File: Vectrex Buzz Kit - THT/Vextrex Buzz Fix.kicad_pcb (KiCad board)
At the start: 2 copper layers, 22.9 x 41.7 mm, 11 parts

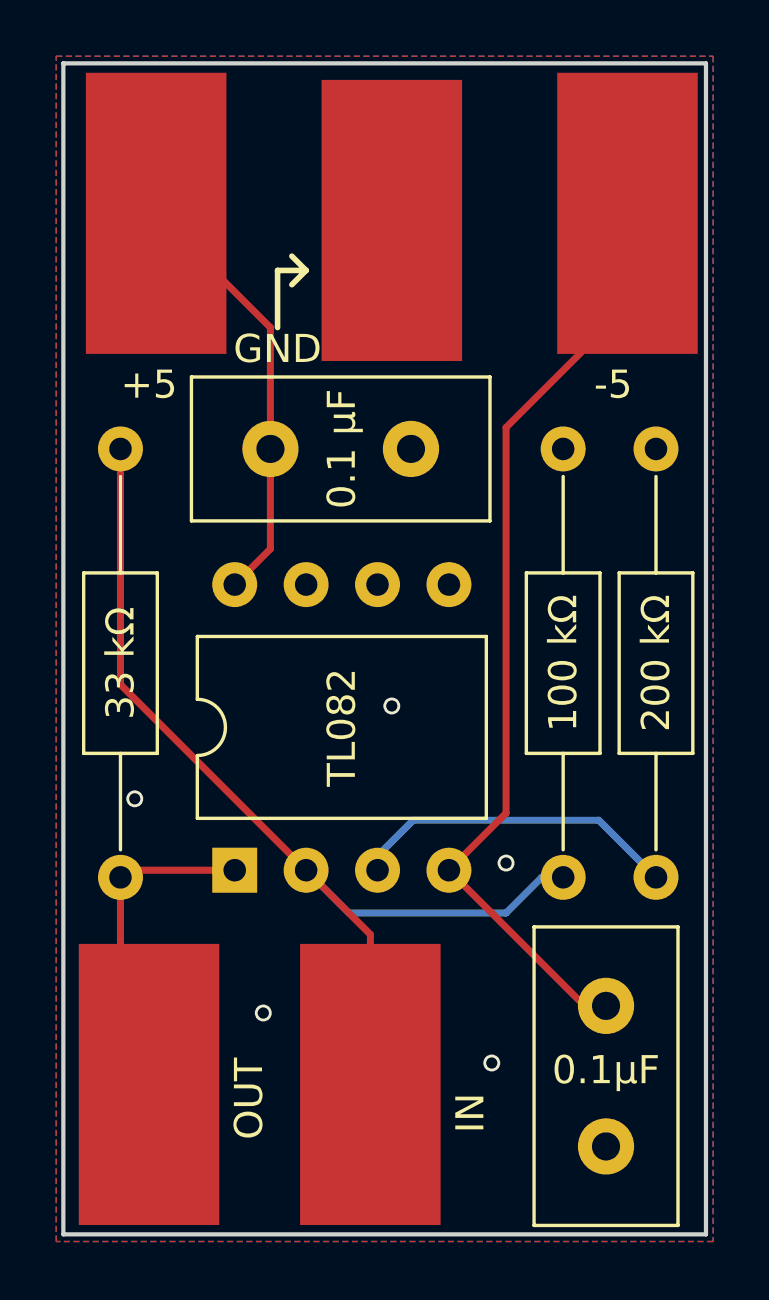
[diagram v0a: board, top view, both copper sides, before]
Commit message: Fixed Unintentional Antenna
Thanks to mobiusstriptech for the fix, applied to both SMD and THT versions.
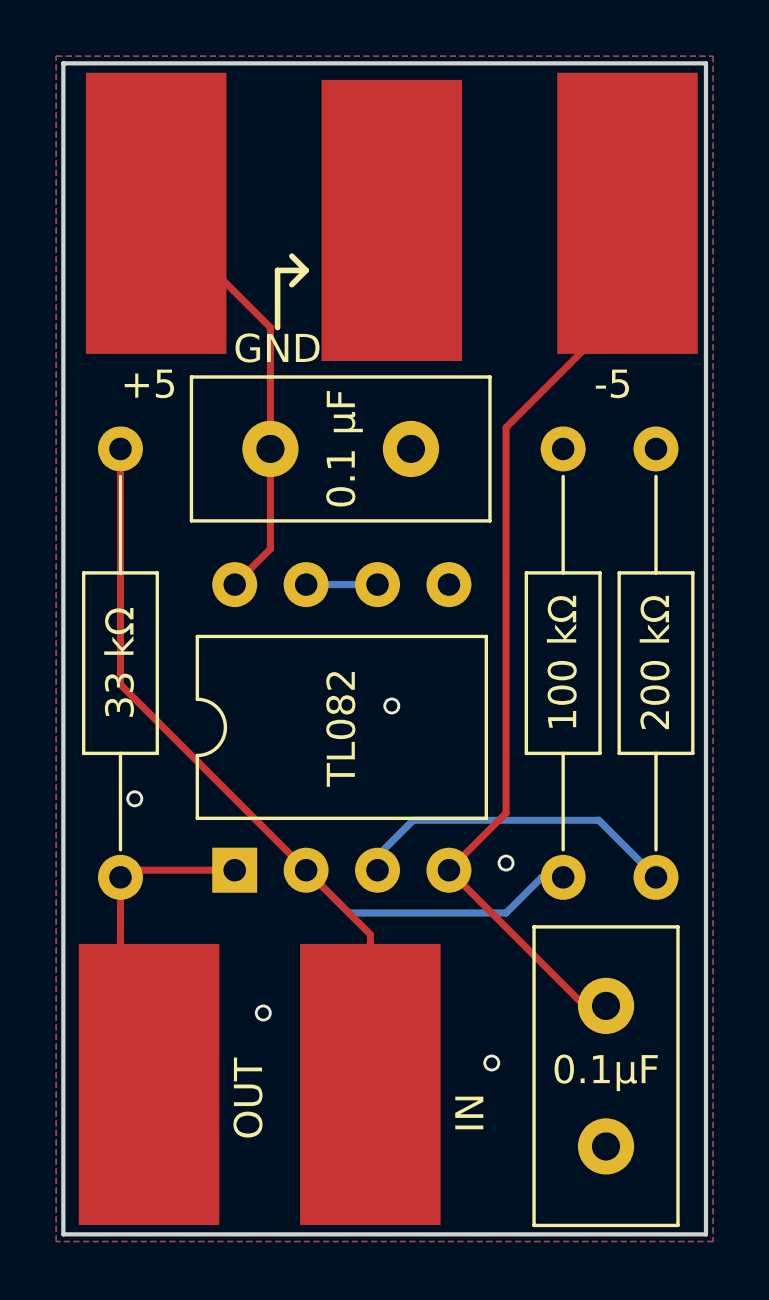
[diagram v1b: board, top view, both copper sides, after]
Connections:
- TL082 pad 5: (no net) -> GND
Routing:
- net (no net): track 0.00 -> 2.54 mm
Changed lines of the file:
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@@
-(kicad_pcb (version 4) (host pcbnew 4.0.7)
+(kicad_pcb (version 20171130) (host pcbnew "(5.1.5)-3")
   (general
-    (links 14)
-    (no_connects 0)
-    (area 143.51 86.614 166.878001 130.615)
     (thickness 1.6)
     (drawings 10)
-    (tracks 31)
+    (tracks 32)
     (zones 0)
     (modules 11)
@@
     (zone_45_only no)
     (trace_min 0.2)
-    (segment_width 0.2)
-    (edge_width 0.15)
     (via_size 0.6)
     (via_drill 0.4)
@@
     (uvia_min_size 0.2)
     (uvia_min_drill 0.1)
+    (edge_width 0.15)
+    (segment_width 0.2)
     (pcb_text_width 0.3)
     (pcb_text_size 1.5 1.5)
@@
     (mod_text_size 1 1)
     (mod_text_width 0.15)
-    (pad_size 1.524 1.524)
-    (pad_drill 0.762)
+    (pad_size 1.6 1.6)
+    (pad_drill 0.8)
     (pad_to_mask_clearance 0.2)
     (aux_axis_origin 0 0)
     (visible_elements 7FFFFFFF)
     (pcbplotparams
-      (layerselection 0x010f0_80000001)
+      (layerselection 0x010f0_ffffffff)
       (usegerberextensions true)
+      (usegerberattributes false)
+      (usegerberadvancedattributes false)
+      (creategerberjobfile false)
       (excludeedgelayer true)
       (linewidth 0.100000)
@@
       (hpglpennumber 1)
       (hpglpenspeed 20)
-      (hpglpendiameter 15)
-      (hpglpenoverlay 2)
+      (hpglpendiameter 15.000000)
       (psnegative false)
       (psa4output false)
@@
       (drillshape 0)
       (scaleselection 1)
-      (outputdirectory gerbers/1.0/))
+      (outputdirectory "gerbers/1.2/"))
   )
   (net 0 "")
@@
     (pad 1 thru_hole rect (at 0 0 90) (size 1.6 1.6) (drill 0.8) (layers *.Cu *.Mask)
       (net 5 OUTPUT))
-    (pad 5 thru_hole oval (at 10.16 7.62 90) (size 1.6 1.6) (drill 0.8) (layers *.Cu *.Mask))
+    (pad 5 thru_hole oval (at 10.16 7.62 90) (size 1.6 1.6) (drill 0.8) (layers *.Cu *.Mask)
+      (net 2 GND))
     (pad 2 thru_hole oval (at 0 2.54 90) (size 1.6 1.6) (drill 0.8) (layers *.Cu *.Mask)
       (net 4 INPUT))
@@
     (descr "C, Disc series, Radial, pin pitch=5.00mm, , diameter*width=10.5*5.0mm^2, Capacitor, http://www.vishay.com/docs/28535/vy2series.pdf")
     (tags "C Disc series Radial pin pitch 5.00mm  diameter 10.5mm width 5.0mm Capacitor")
-    (fp_text reference 0.1μF (at 2.286 0 360) (layer F.SilkS)
+    (fp_text reference 0.1μF (at 2.286 0) (layer F.SilkS)
       (effects (font (size 1 1) (thickness 0.15)))
     )
@@
   (gr_line (start 166.624 128.524) (end 143.764 128.524) (angle 90) (layer Edge.Cuts) (width 0.15))
   (gr_line (start 166.624 86.868) (end 166.624 128.524) (angle 90) (layer Edge.Cuts) (width 0.15))
+  (segment (start 152.4 105.41) (end 154.94 105.41) (width 0.25) (layer B.Cu) (net 0))
   (segment (start 151.13 100.584) (end 151.13 96.266) (width 0.25) (layer F.Cu) (net 1))
   (segment (start 151.13 96.266) (end 147.066 92.202) (width 0.25) (layer F.Cu) (net 1))
